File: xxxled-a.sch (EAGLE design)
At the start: 9 parts, among them J2 BAT+, J3 LED-, J4 BAT+, J5 LED-, Q1 TIP120

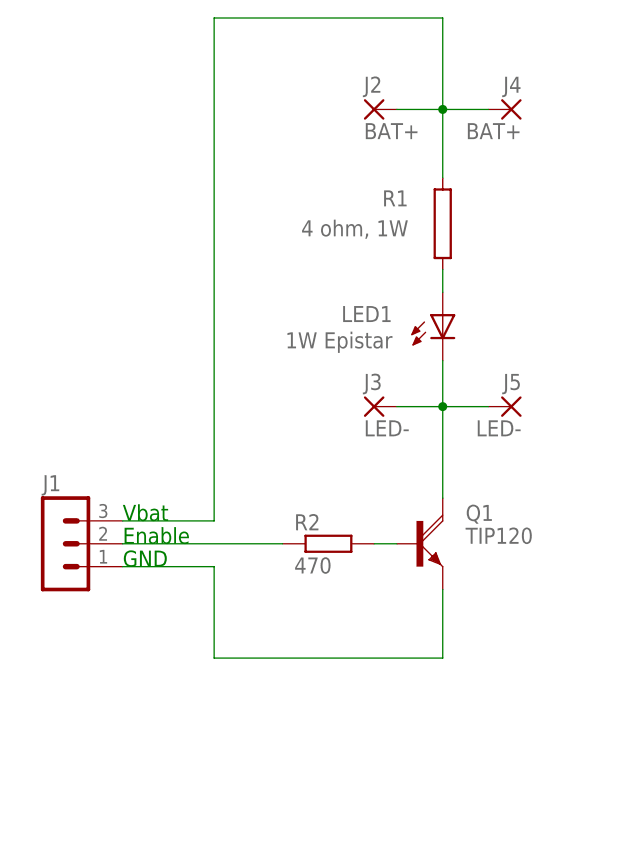
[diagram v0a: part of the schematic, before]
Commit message: First draft single-sided PCB layout
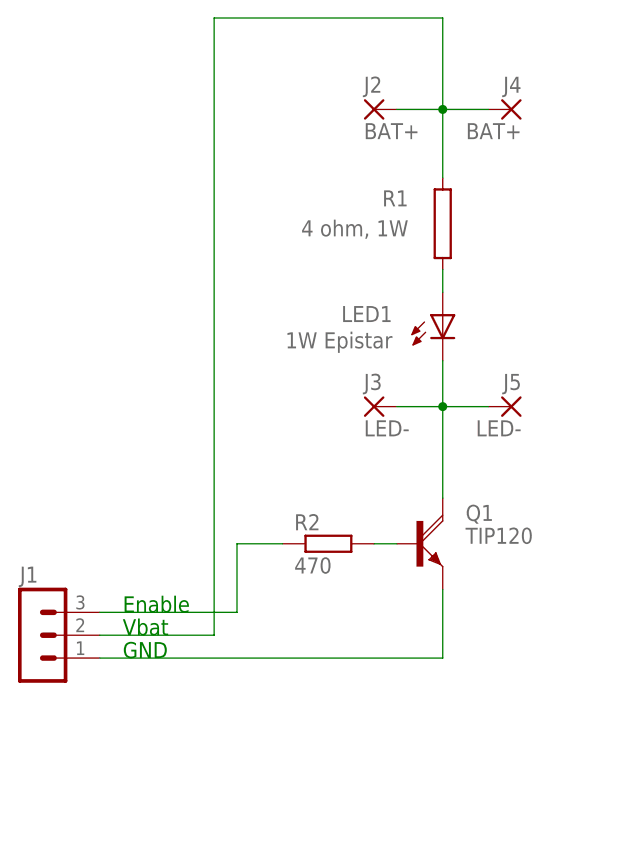
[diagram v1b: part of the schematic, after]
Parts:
- LED1: device xxxled:W49180 -> xxxled:W49180EDGE
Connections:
- net N$1: now also J1.3; no longer J1.2
- net N$5: now also J1.2; no longer J1.3
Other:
- moved on the sheet: J1
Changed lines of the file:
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@@
 <part name="R1" library="resistor-power" deviceset="R" device="AC01" value="4 ohm, 1W"/>
 <part name="J1" library="con-lstb" deviceset="MA03-1" device=""/>
-<part name="LED1" library="xxxled" deviceset="W49180" device="" value="1W Epistar"/>
+<part name="LED1" library="xxxled" deviceset="W49180" device="EDGE" value="1W Epistar"/>
 <part name="R2" library="resistor" deviceset="R-EU_" device="0207/12" value="470"/>
 <part name="J2" library="wirepad" deviceset="WIREPAD" device="2,54/1,1" value="BAT+"/>
@@
 <text x="152.4" y="27.94" size="2.54" layer="97">Straightedge LED Board</text>
 <text x="238.76" y="7.62" size="2.54" layer="97">A</text>
-<text x="99.06" y="81.28" size="1.778" layer="91">Vbat</text>
-<text x="99.06" y="76.2" size="1.778" layer="91">GND</text>
-<text x="99.06" y="78.74" size="1.778" layer="91">Enable</text>
+<text x="99.06" y="68.58" size="1.778" layer="91">Vbat</text>
+<text x="99.06" y="66.04" size="1.778" layer="91">GND</text>
+<text x="99.06" y="71.12" size="1.778" layer="91">Enable</text>
 </plain>
 <instances>
@@
 <attribute name="VALUE" x="130.81" y="114.681" size="1.778" layer="96" rot="R180"/>
 </instance>
-<instance part="J1" gate="G$1" x="91.44" y="78.74"/>
+<instance part="J1" gate="G$1" x="88.9" y="68.58"/>
 <instance part="LED1" gate="G$1" x="134.62" y="104.14" smashed="yes">
 <attribute name="NAME" x="129.032" y="105.156" size="1.778" layer="95" rot="R180"/>
@@
 </busses>
 <nets>
-<net name="N$1" class="0">
-<segment>
-<pinref part="J1" gate="G$1" pin="2"/>
-<pinref part="R2" gate="G$1" pin="1"/>
-<wire x1="99.06" y1="78.74" x2="116.84" y2="78.74" width="0.1524" layer="91"/>
-</segment>
-</net>
 <net name="N$2" class="0">
 <segment>
@@
 <wire x1="134.62" y1="119.38" x2="134.62" y2="127" width="0.1524" layer="91"/>
 <junction x="134.62" y="127"/>
-<pinref part="J1" gate="G$1" pin="3"/>
-<wire x1="99.06" y1="81.28" x2="109.22" y2="81.28" width="0.1524" layer="91"/>
-<wire x1="109.22" y1="81.28" x2="109.22" y2="137.16" width="0.1524" layer="91"/>
 <wire x1="109.22" y1="137.16" x2="134.62" y2="137.16" width="0.1524" layer="91"/>
 <wire x1="134.62" y1="137.16" x2="134.62" y2="127" width="0.1524" layer="91"/>
 <pinref part="J2" gate="G$1" pin="P"/>
 <pinref part="J4" gate="G$1" pin="P"/>
+<wire x1="109.22" y1="137.16" x2="109.22" y2="68.58" width="0.1524" layer="91"/>
+<pinref part="J1" gate="G$1" pin="2"/>
+<wire x1="109.22" y1="68.58" x2="96.52" y2="68.58" width="0.1524" layer="91"/>
 </segment>
 </net>
@@
 <pinref part="Q1" gate="1" pin="E"/>
 <wire x1="134.62" y1="73.66" x2="134.62" y2="66.04" width="0.1524" layer="91"/>
-<wire x1="134.62" y1="66.04" x2="109.22" y2="66.04" width="0.1524" layer="91"/>
-<wire x1="109.22" y1="66.04" x2="109.22" y2="76.2" width="0.1524" layer="91"/>
+<wire x1="134.62" y1="66.04" x2="96.52" y2="66.04" width="0.1524" layer="91"/>
 <pinref part="J1" gate="G$1" pin="1"/>
-<wire x1="109.22" y1="76.2" x2="99.06" y2="76.2" width="0.1524" layer="91"/>
 </segment>
 </net>
+<net name="N$1" class="0">
+<segment>
+<pinref part="J1" gate="G$1" pin="3"/>
+<wire x1="96.52" y1="71.12" x2="111.76" y2="71.12" width="0.1524" layer="91"/>
+<wire x1="111.76" y1="71.12" x2="111.76" y2="78.74" width="0.1524" layer="91"/>
+<pinref part="R2" gate="G$1" pin="1"/>
+<wire x1="111.76" y1="78.74" x2="116.84" y2="78.74" width="0.1524" layer="91"/>
+</segment>
+</net>

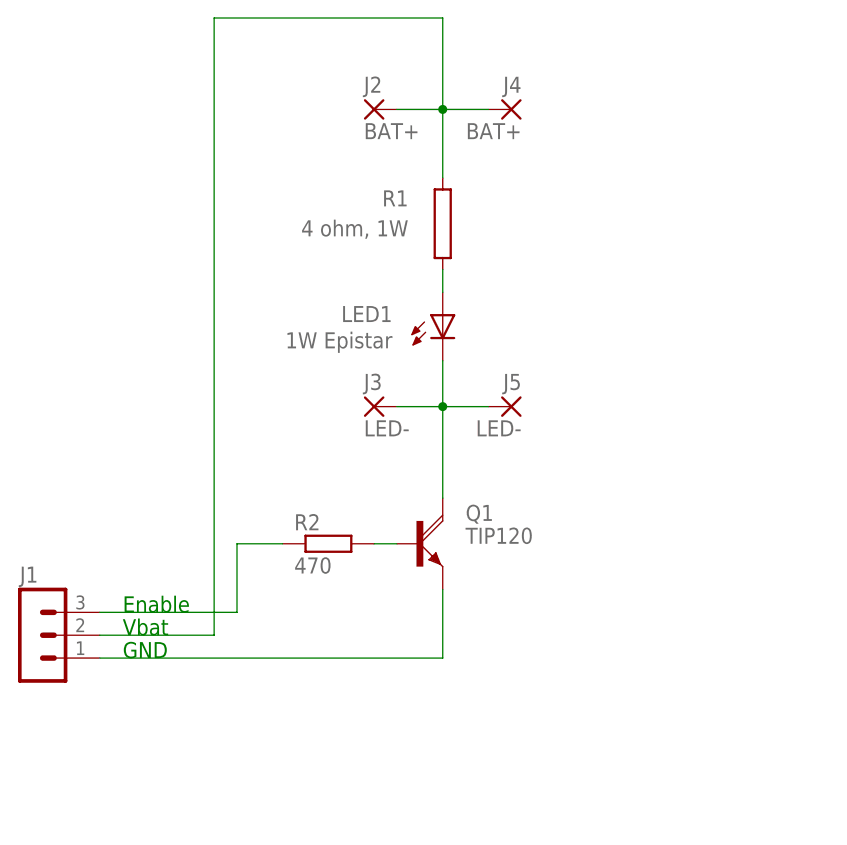
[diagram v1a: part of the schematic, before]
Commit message: * added J2 to connect the two board clusters on one stake to each other * Tidied silkscreen layout * Moved mounting holes (and Q1) in a bit * Layout with all 50mil traces * Down to 1/2W for R1, still plenty and this saves money and space
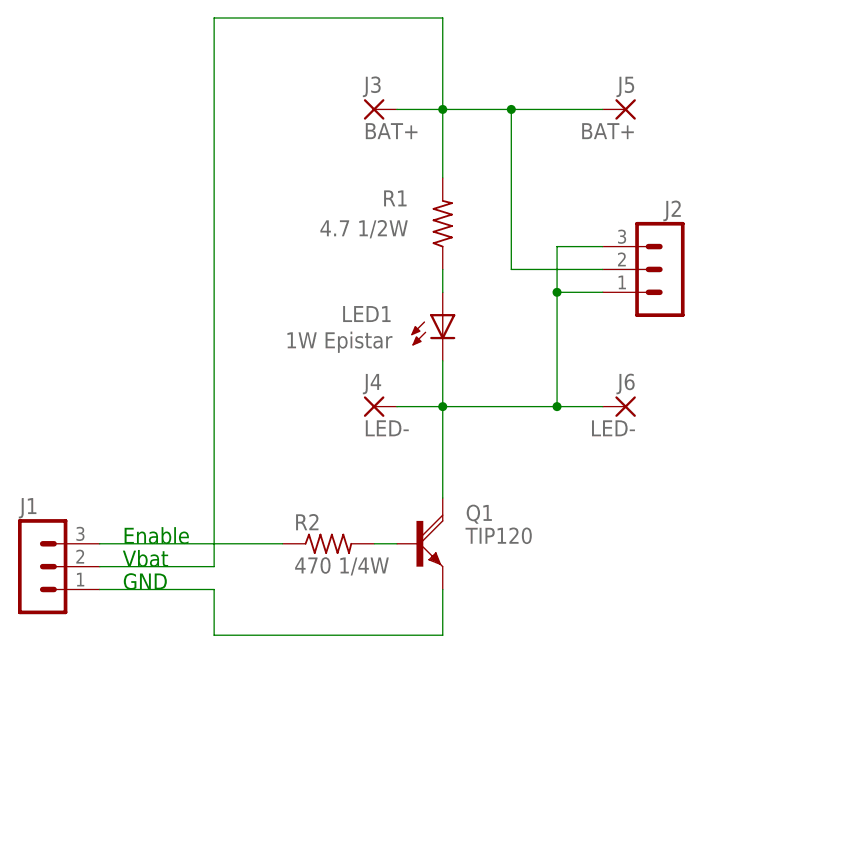
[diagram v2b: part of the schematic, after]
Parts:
- added J6: LED-, wirepad:WIREPAD2,54/1,1
- J2: value BAT+ -> (none); device wirepad:WIREPAD2,54/1,1 -> con-lstb:MA03-1
- J3, J5: value LED- -> BAT+
- J4: value BAT+ -> LED-
- R1: value 4 ohm, 1W -> 4.7 1/2W; device resistor-power:RAC01 -> resistor:R-US_0309/12
- R2: value 470 -> 470 1/4W; device resistor:R-EU_0207/12 -> resistor:R-US_0207/10
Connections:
- net N$3: now also J2.1, J2.3, J4.P, J6.P; no longer J3.P, J5.P
- net N$5: now also J2.2, J3.P, J5.P; no longer J2.P, J4.P
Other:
- moved on the sheet: J1, J3, J4, J5
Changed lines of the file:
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@@
 <part name="FRAME1" library="frames" deviceset="LETTER_L" device=""/>
 <part name="Q1" library="xxxled" deviceset="TIP120" device=""/>
-<part name="R1" library="resistor-power" deviceset="R" device="AC01" value="4 ohm, 1W"/>
+<part name="R1" library="resistor" deviceset="R-US_" device="0309/12" value="4.7 1/2W"/>
 <part name="J1" library="con-lstb" deviceset="MA03-1" device=""/>
 <part name="LED1" library="xxxled" deviceset="W49180" device="EDGE" value="1W Epistar"/>
-<part name="R2" library="resistor" deviceset="R-EU_" device="0207/12" value="470"/>
-<part name="J2" library="wirepad" deviceset="WIREPAD" device="2,54/1,1" value="BAT+"/>
-<part name="J3" library="wirepad" deviceset="WIREPAD" device="2,54/1,1" value="LED-"/>
-<part name="J4" library="wirepad" deviceset="WIREPAD" device="2,54/1,1" value="BAT+"/>
-<part name="J5" library="wirepad" deviceset="WIREPAD" device="2,54/1,1" value="LED-"/>
+<part name="R2" library="resistor" deviceset="R-US_" device="0207/10" value="470 1/4W"/>
+<part name="J3" library="wirepad" deviceset="WIREPAD" device="2,54/1,1" value="BAT+"/>
+<part name="J4" library="wirepad" deviceset="WIREPAD" device="2,54/1,1" value="LED-"/>
+<part name="J5" library="wirepad" deviceset="WIREPAD" device="2,54/1,1" value="BAT+"/>
+<part name="J6" library="wirepad" deviceset="WIREPAD" device="2,54/1,1" value="LED-"/>
+<part name="J2" library="con-lstb" deviceset="MA03-1" device=""/>
 </parts>
 <sheets>
@@
 <text x="152.4" y="27.94" size="2.54" layer="97">Straightedge LED Board</text>
 <text x="238.76" y="7.62" size="2.54" layer="97">A</text>
-<text x="99.06" y="68.58" size="1.778" layer="91">Vbat</text>
-<text x="99.06" y="66.04" size="1.778" layer="91">GND</text>
-<text x="99.06" y="71.12" size="1.778" layer="91">Enable</text>
+<text x="99.06" y="76.2" size="1.778" layer="91">Vbat</text>
+<text x="99.06" y="73.66" size="1.778" layer="91">GND</text>
+<text x="99.06" y="78.74" size="1.778" layer="91">Enable</text>
 </plain>
 <instances>
@@
 <attribute name="VALUE" x="130.81" y="114.681" size="1.778" layer="96" rot="R180"/>
 </instance>
-<instance part="J1" gate="G$1" x="88.9" y="68.58"/>
+<instance part="J1" gate="G$1" x="88.9" y="76.2"/>
 <instance part="LED1" gate="G$1" x="134.62" y="104.14" smashed="yes">
 <attribute name="NAME" x="129.032" y="105.156" size="1.778" layer="95" rot="R180"/>
@@
 </instance>
 <instance part="R2" gate="G$1" x="121.92" y="78.74"/>
-<instance part="J2" gate="G$1" x="127" y="127"/>
-<instance part="J3" gate="G$1" x="127" y="93.98"/>
-<instance part="J4" gate="G$1" x="142.24" y="127" rot="MR0"/>
-<instance part="J5" gate="G$1" x="142.24" y="93.98" rot="MR0"/>
+<instance part="J3" gate="G$1" x="127" y="127"/>
+<instance part="J4" gate="G$1" x="127" y="93.98"/>
+<instance part="J5" gate="G$1" x="154.94" y="127" rot="MR0"/>
+<instance part="J6" gate="G$1" x="154.94" y="93.98" rot="MR0"/>
+<instance part="J2" gate="G$1" x="160.02" y="109.22" rot="MR0"/>
 </instances>
 <busses>
@@
 <wire x1="129.54" y1="93.98" x2="134.62" y2="93.98" width="0.1524" layer="91"/>
 <junction x="134.62" y="93.98"/>
-<wire x1="134.62" y1="93.98" x2="139.7" y2="93.98" width="0.1524" layer="91"/>
-<pinref part="J5" gate="G$1" pin="P"/>
-<pinref part="J3" gate="G$1" pin="P"/>
+<wire x1="134.62" y1="93.98" x2="147.32" y2="93.98" width="0.1524" layer="91"/>
+<pinref part="J6" gate="G$1" pin="P"/>
+<pinref part="J4" gate="G$1" pin="P"/>
+<wire x1="147.32" y1="93.98" x2="152.4" y2="93.98" width="0.1524" layer="91"/>
+<wire x1="147.32" y1="93.98" x2="147.32" y2="106.68" width="0.1524" layer="91"/>
+<pinref part="J2" gate="G$1" pin="1"/>
+<wire x1="147.32" y1="106.68" x2="152.4" y2="106.68" width="0.1524" layer="91"/>
+<pinref part="J2" gate="G$1" pin="3"/>
+<wire x1="152.4" y1="111.76" x2="147.32" y2="111.76" width="0.1524" layer="91"/>
+<wire x1="147.32" y1="111.76" x2="147.32" y2="106.68" width="0.1524" layer="91"/>
+<junction x="147.32" y="106.68"/>
+<junction x="147.32" y="93.98"/>
 </segment>
 </net>
@@
 <wire x1="129.54" y1="127" x2="134.62" y2="127" width="0.1524" layer="91"/>
 <pinref part="R1" gate="G$1" pin="2"/>
-<wire x1="134.62" y1="127" x2="139.7" y2="127" width="0.1524" layer="91"/>
+<wire x1="134.62" y1="127" x2="142.24" y2="127" width="0.1524" layer="91"/>
+<wire x1="142.24" y1="127" x2="152.4" y2="127" width="0.1524" layer="91"/>
 <wire x1="134.62" y1="119.38" x2="134.62" y2="127" width="0.1524" layer="91"/>
 <junction x="134.62" y="127"/>
 <wire x1="109.22" y1="137.16" x2="134.62" y2="137.16" width="0.1524" layer="91"/>
 <wire x1="134.62" y1="137.16" x2="134.62" y2="127" width="0.1524" layer="91"/>
-<pinref part="J2" gate="G$1" pin="P"/>
-<pinref part="J4" gate="G$1" pin="P"/>
-<wire x1="109.22" y1="137.16" x2="109.22" y2="68.58" width="0.1524" layer="91"/>
+<pinref part="J3" gate="G$1" pin="P"/>
+<pinref part="J5" gate="G$1" pin="P"/>
+<wire x1="109.22" y1="137.16" x2="109.22" y2="76.2" width="0.1524" layer="91"/>
 <pinref part="J1" gate="G$1" pin="2"/>
-<wire x1="109.22" y1="68.58" x2="96.52" y2="68.58" width="0.1524" layer="91"/>
+<wire x1="109.22" y1="76.2" x2="96.52" y2="76.2" width="0.1524" layer="91"/>
+<pinref part="J2" gate="G$1" pin="2"/>
+<wire x1="152.4" y1="109.22" x2="142.24" y2="109.22" width="0.1524" layer="91"/>
+<wire x1="142.24" y1="109.22" x2="142.24" y2="127" width="0.1524" layer="91"/>
+<junction x="142.24" y="127"/>
 </segment>
 </net>
@@
 <segment>
 <pinref part="Q1" gate="1" pin="E"/>
-<wire x1="134.62" y1="73.66" x2="134.62" y2="66.04" width="0.1524" layer="91"/>
-<wire x1="134.62" y1="66.04" x2="96.52" y2="66.04" width="0.1524" layer="91"/>
+<wire x1="134.62" y1="73.66" x2="134.62" y2="68.58" width="0.1524" layer="91"/>
 <pinref part="J1" gate="G$1" pin="1"/>
+<wire x1="96.52" y1="73.66" x2="109.22" y2="73.66" width="0.1524" layer="91"/>
+<wire x1="109.22" y1="73.66" x2="109.22" y2="68.58" width="0.1524" layer="91"/>
+<wire x1="109.22" y1="68.58" x2="134.62" y2="68.58" width="0.1524" layer="91"/>
 </segment>
 </net>
@@
 <segment>
 <pinref part="J1" gate="G$1" pin="3"/>
-<wire x1="96.52" y1="71.12" x2="111.76" y2="71.12" width="0.1524" layer="91"/>
-<wire x1="111.76" y1="71.12" x2="111.76" y2="78.74" width="0.1524" layer="91"/>
+<wire x1="96.52" y1="78.74" x2="116.84" y2="78.74" width="0.1524" layer="91"/>
 <pinref part="R2" gate="G$1" pin="1"/>
-<wire x1="111.76" y1="78.74" x2="116.84" y2="78.74" width="0.1524" layer="91"/>
 </segment>
 </net>

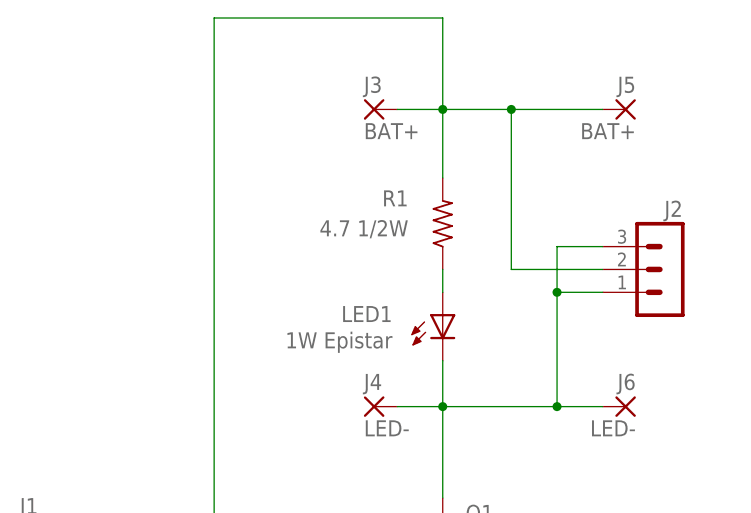
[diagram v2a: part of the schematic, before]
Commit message: Switch to 2.7 ohm power resistor
With the prototype PCB and 4 LEDs, this gives a peak current of ~0.75 A at 4.5V
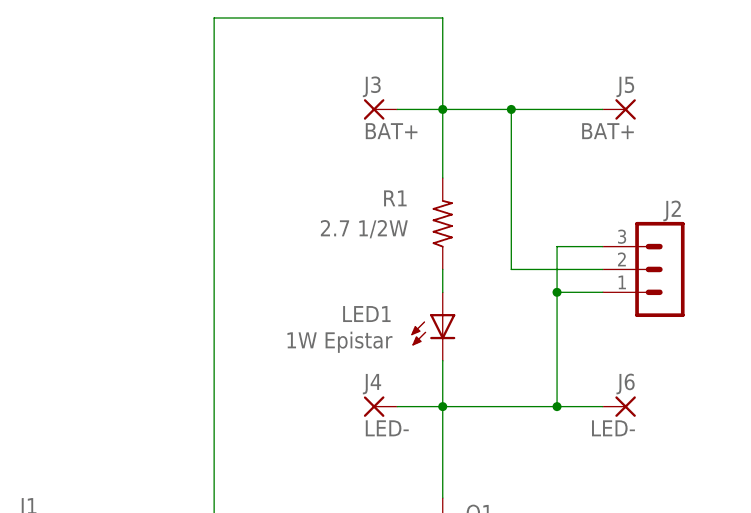
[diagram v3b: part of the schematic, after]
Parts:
- R1: value 4.7 1/2W -> 2.7 1/2W
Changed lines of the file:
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@@
 <part name="FRAME1" library="frames" deviceset="LETTER_L" device=""/>
 <part name="Q1" library="xxxled" deviceset="TIP120" device=""/>
-<part name="R1" library="resistor" deviceset="R-US_" device="0309/12" value="4.7 1/2W"/>
+<part name="R1" library="resistor" deviceset="R-US_" device="0309/12" value="2.7 1/2W"/>
 <part name="J1" library="con-lstb" deviceset="MA03-1" device=""/>
 <part name="LED1" library="xxxled" deviceset="W49180" device="EDGE" value="1W Epistar"/>
